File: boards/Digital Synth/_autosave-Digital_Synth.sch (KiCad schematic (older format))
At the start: 32 parts, among them J5 Barrel_Jack, J6 JTAG, J7 Micro_SD_Card, SW1 SW_Push, SW2 SW_Push, U1 LM1117-3.3, U5 STM32F405RGTx, Y1 12MHz

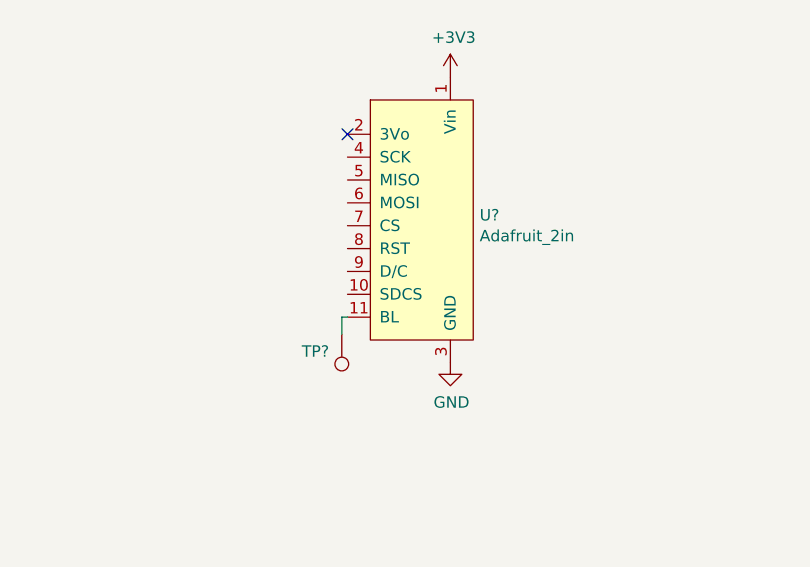
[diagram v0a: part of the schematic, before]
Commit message: finished routing to avr
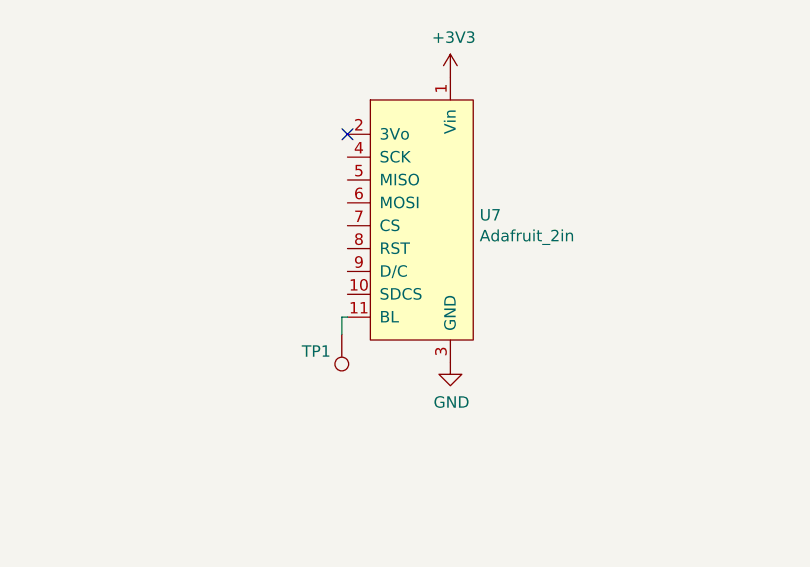
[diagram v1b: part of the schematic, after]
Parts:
- gave numbers to parts that had none: 2
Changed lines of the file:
@@
 NoConn ~ 8950 3350
 $Comp
-L power:GND #PWR?
+L power:GND #PWR0110
 U 1 1 623F4583
 P 9400 4350
-F 0 "#PWR?" H 9400 4100 50  0001 C CNN
+F 0 "#PWR0110" H 9400 4100 50  0001 C CNN
 F 1 "GND" H 9405 4177 50  0000 C CNN
 F 2 "" H 9400 4350 50  0001 C CNN
@@
 $EndComp
 $Comp
-L power:+3V3 #PWR?
+L power:+3V3 #PWR0111
 U 1 1 623ECA3D
 P 9400 3100
-F 0 "#PWR?" H 9400 2950 50  0001 C CNN
+F 0 "#PWR0111" H 9400 2950 50  0001 C CNN
 F 1 "+3V3" H 9415 3273 50  0000 C CNN
 F 2 "" H 9400 3100 50  0001 C CNN
@@
 $EndComp
 $Comp
-L Connector:TestPoint TP?
+L Connector:TestPoint TP1
 U 1 1 6240D6CD
 P 8925 4225
-F 0 "TP?" H 9100 4300 50  0000 R CNN
+F 0 "TP1" H 9100 4300 50  0000 R CNN
 F 1 "TestPoint" H 8867 4342 50  0001 R CNN
 F 2 "" H 9125 4225 50  0001 C CNN
@@
 $EndComp
 $Comp
-L Display_Graphic:Adafruit_2in U?
+L Display_Graphic:Adafruit_2in U7
 U 1 1 623EB93B
 P 9050 3150
-F 0 "U?" H 9528 2596 50  0000 L CNN
+F 0 "U7" H 9528 2596 50  0000 L CNN
 F 1 "Adafruit_2in" H 9528 2505 50  0000 L CNN
 F 2 "" H 8900 3150 50  0001 C CNN
